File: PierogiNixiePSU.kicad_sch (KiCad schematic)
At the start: 18 parts, among them J1 OSTVN02A150, J2 OSTVN02A150, J3 PJ-202A, U1 MAX1771CSAT

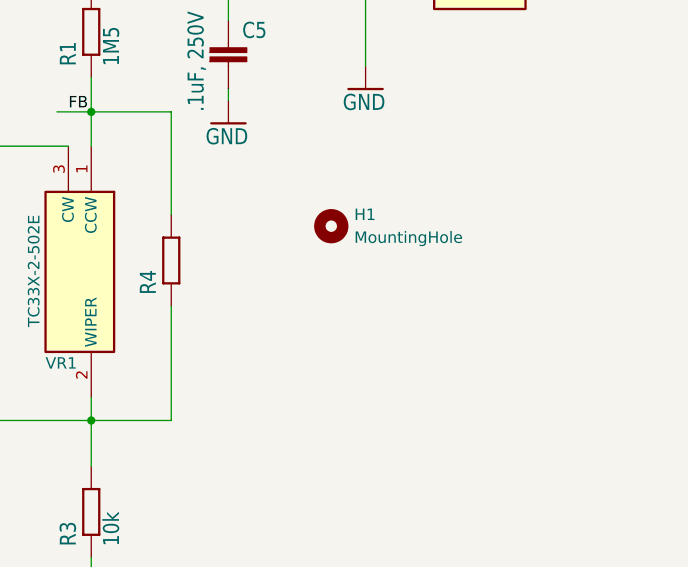
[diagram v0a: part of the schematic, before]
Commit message: Added mounting hole
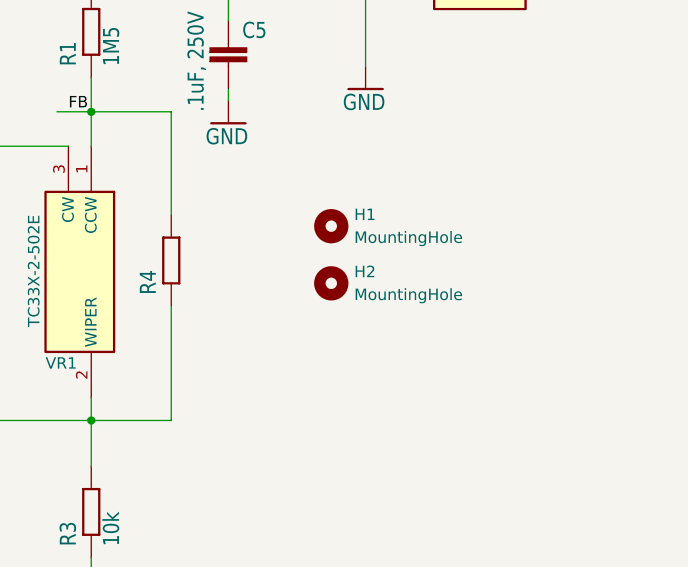
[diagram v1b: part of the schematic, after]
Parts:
- added H2: MountingHole, MountingHole:MountingHole_3.5mm_Pad_Via, symbol Mechanical:MountingHole
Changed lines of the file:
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@@
+    )
+  )
+  (symbol (lib_id "Mechanical:MountingHole") (at 232.41 111.76 0) (unit 1)
+    (in_bom yes) (on_board yes) (dnp no) (fields_autoplaced)
+    (property "Reference" "H2" (at 234.95 110.49 0)
+      (effects (font (size 1.27 1.27)) (justify left))
+    )
+    (property "Value" "MountingHole" (at 234.95 113.03 0)
+      (effects (font (size 1.27 1.27)) (justify left))
+    )
+    (property "Footprint" "MountingHole:MountingHole_3.5mm_Pad_Via" (at 232.41 111.76 0)
+      (effects (font (size 1.27 1.27)) hide)
+    )
+    (property "Datasheet" "~" (at 232.41 111.76 0)
+      (effects (font (size 1.27 1.27)) hide)
+    )
+    (instances
+      (project "PierogiNixiePSU"
+        (path "/aae08d1b-aae6-480a-b174-6c54c1927943"
+          (reference "H2") (unit 1)
+        )
+      )
     )
   )

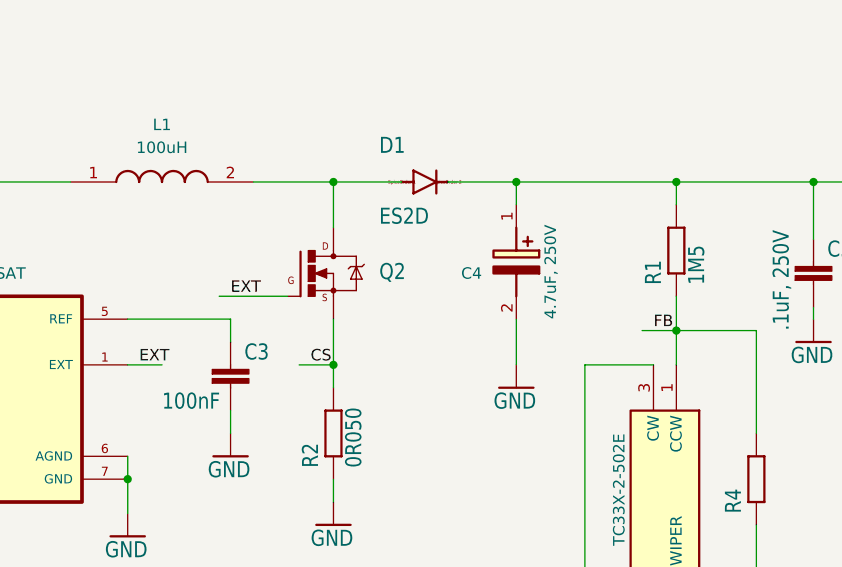
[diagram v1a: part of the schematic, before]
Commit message: Updated schematic and fixed thickness of GND traces
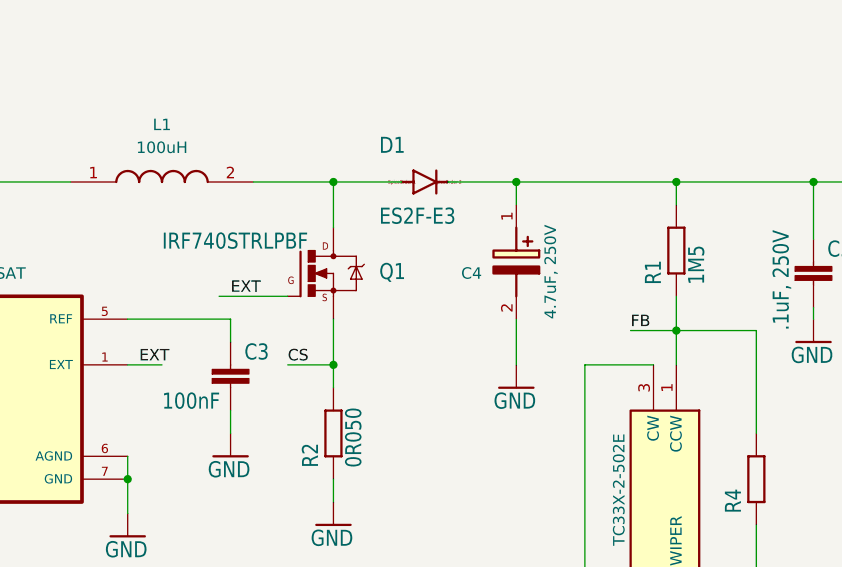
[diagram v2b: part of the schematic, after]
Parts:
- D1: value ES2D -> ES2F-E3
- Q1: renamed from Q2; value ~ -> IRF740STRLPBF
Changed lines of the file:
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@@
-    (stroke (width 0) (type default))
-  )
-  (wire (pts (xy 201.93 92.71) (xy 205.74 92.71))
     (stroke (width 0) (type default))
   )
@@
     (stroke (width 0) (type default))
   )
+  (wire (pts (xy 200.66 92.71) (xy 205.74 92.71))
+    (stroke (width 0) (type default))
+  )
   (wire (pts (xy 236.22 78.74) (xy 238.76 78.74))
     (stroke (width 0.1524) (type solid))
@@
     (stroke (width 0.1524) (type solid))
   )
-  (wire (pts (xy 163.83 96.52) (xy 167.64 96.52))
+  (wire (pts (xy 162.56 96.52) (xy 167.64 96.52))
     (stroke (width 0) (type default))
   )
@@
     (effects (font (size 1.27 1.27)) (justify left bottom))
   )
-  (label "FB" (at 203.2 92.71 0) (fields_autoplaced)
+  (label "FB" (at 200.66 92.71 0) (fields_autoplaced)
     (effects (font (size 1.27 1.27)) (justify left bottom))
   )
-  (label "CS" (at 165.1 96.52 0) (fields_autoplaced)
+  (label "CS" (at 162.56 96.52 0) (fields_autoplaced)
     (effects (font (size 1.27 1.27)) (justify left bottom))
   )
@@
       (effects (font (size 1.778 1.5113)) (justify left bottom))
     )
-    (property "Value" "ES2D" (at 172.72 81.0514 0)
+    (property "Value" "ES2F-E3" (at 172.72 81.0514 0)
       (effects (font (size 1.778 1.5113)) (justify left bottom))
     )
@@
   )
   (symbol (lib_id "EL35901-eagle-import:IRF740ADPAK") (at 165.1 86.36 0) (unit 1)
-    (in_bom yes) (on_board yes) (dnp no) (fields_autoplaced)
-    (property "Reference" "Q2" (at 172.72 86.1631 0)
+    (in_bom yes) (on_board yes) (dnp no)
+    (property "Reference" "Q1" (at 172.72 86.1631 0)
       (effects (font (size 1.778 1.5113)) (justify left))
     )
-    (property "Value" "~" (at 172.72 86.36 0)
+    (property "Value" "IRF740STRLPBF" (at 148.59 83.82 0)
       (effects (font (size 1.778 1.5113)) (justify left bottom))
     )
@@
       (project "PierogiNixiePSU"
         (path "/aae08d1b-aae6-480a-b174-6c54c1927943"
-          (reference "Q2") (unit 1)
-        )
-      )
+          (reference "Q1") (unit 1)
+        )
+      )
